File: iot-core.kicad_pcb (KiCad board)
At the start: 2 copper layers, 34.3 x 61 mm, 50 parts, among them P1 USB, P10 CONN_01X01, P11 CONN_01X01, P2 CONN_01X02, P3 CONN_01X16, P4 CONN_01X04, P5 CONN_01X16, P6 CONN_01X03, P7 CONN_01X03, P8 CONN_01X01, P9 CONN_01X01, SW1 RST, U1 LP2985LV, U2 STM32F103C8Tx, U3 ESP-07v2, Y1 8MHz

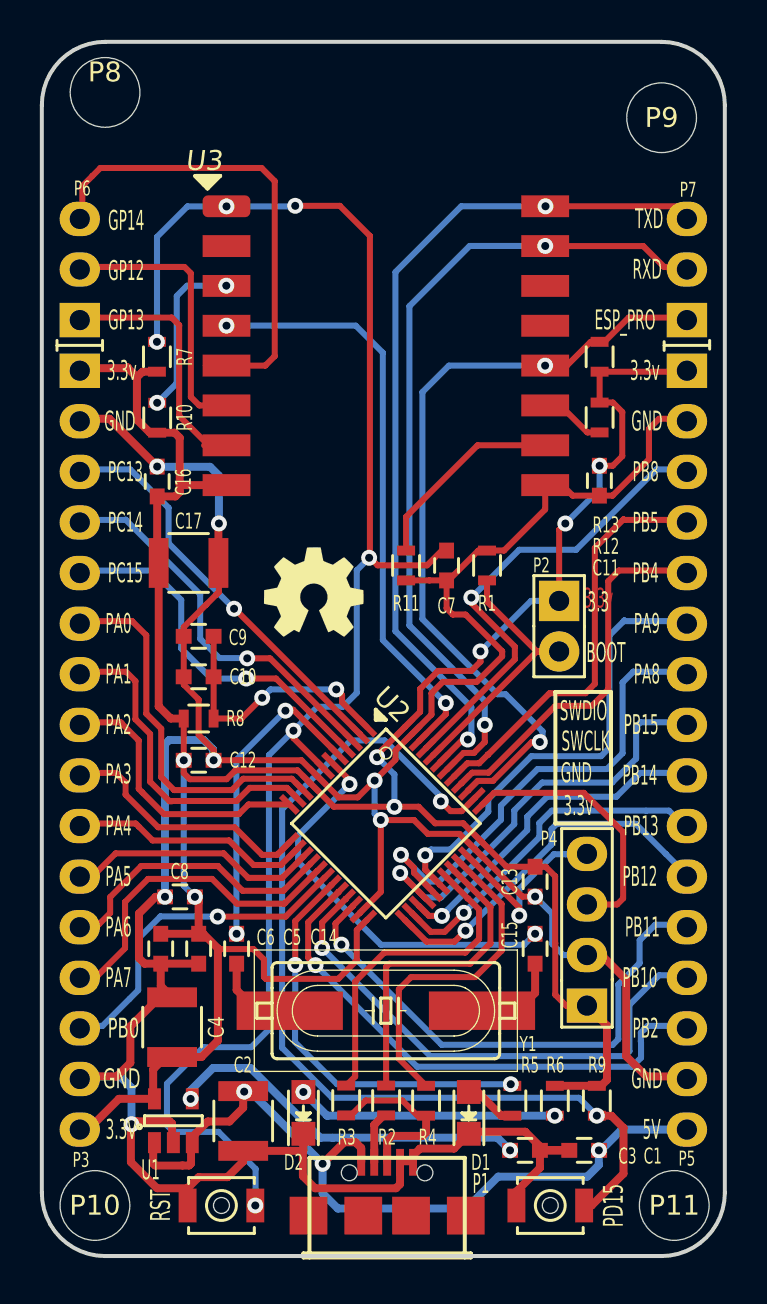
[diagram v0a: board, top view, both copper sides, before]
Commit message: Fix DAO DONG THACH ANH KHONG NOI GND, pin ESP_PRO to PB0, GPIO16 to PB11,DELETE header BOOT 0
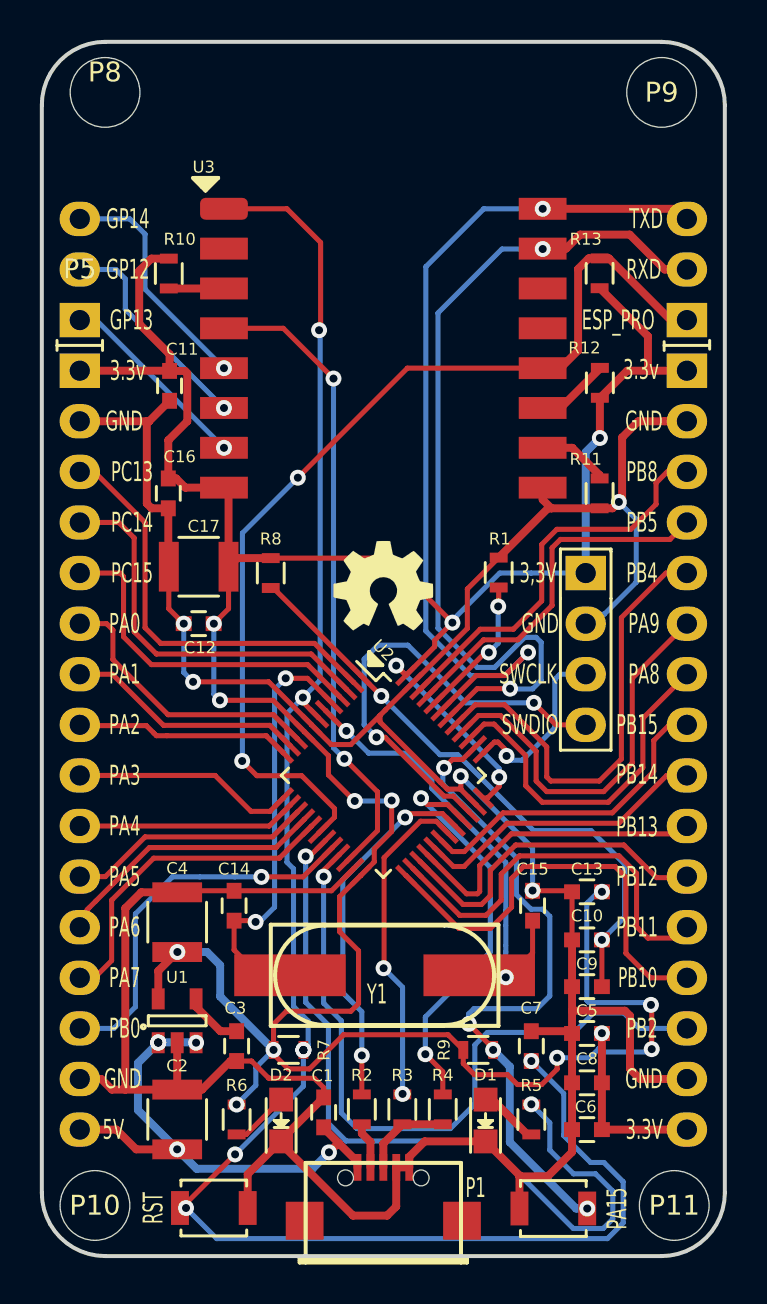
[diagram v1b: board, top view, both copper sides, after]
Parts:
- removed P2: CONN_01X02, Pin_Headers:Pin_Header_Straight_1x02
- removed PD15: SW_PUSH_SMALL_H, Buttons_Switches_SMD:SW_SPST_B3U-1000P-B
- removed SW1: RST, Buttons_Switches_SMD:SW_SPST_B3U-1000P-B
- added PA15: SW_PUSH_SMALL_H, Buttons_Switches_SMD:SW_SPST_B3U-1000P-B, F.Cu at (130.5, 133.5)
- added RST: RST, Buttons_Switches_SMD:SW_SPST_B3U-1000P-B, F.Cu at (113.4, 133.5)
- U2: footprint stm32f108:LQFP48 -> Housings_QFP:LQFP-48_7x7mm_Pitch0.5mm
- Y1: footprint crystal:crystal-HC49UP -> Crystal:HC49_sm
- moved R7 35.4 mm to (117.2, 125.5), turned to 180 degrees
- moved P3 30.5 mm to (137.2, 91.4)
- moved P5 30.5 mm to (106.7, 91.4)
- moved C9 26.3 mm to (132.1, 122.4)
- moved C7 24.5 mm to (129.3, 125.3), turned to 90 degrees
- moved C10 23.5 mm to (132.1, 120.0)
- moved C6 23.2 mm to (132.1, 129.5), turned to 0 degrees
- moved C8 22.5 mm to (132.1, 127.2)
- moved C11 22.1 mm to (111.2, 92.2)
- moved P4 21.7 mm to (132.1, 101.6), turned to 0 degrees
- moved C5 20.0 mm to (132.1, 124.7), turned to 0 degrees
- moved R6 16.0 mm to (114.6, 129.0)
- moved C3 15.4 mm to (114.6, 125.3), turned to 270 degrees
- moved C1 13.2 mm to (118.9, 128.7), turned to 90 degrees
- moved R11 10.4 mm to (132.8, 97.6)
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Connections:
- net IO-13 renamed PB2
- C14 pad 2: Net-(C14-Pad2) -> GNDREF
- C15 pad 2: Net-(C15-Pad2) -> GNDREF
- P3 pad 10: IO-7 -> PB15
- P3 pad 11: IO-8 -> PB14
- P3 pad 12: IO-9 -> PB13
- P3 pad 13: IO-10 -> PB12
- P3 pad 14: IO-11 -> PB10
- P3 pad 3: IO-0 -> PB9
- P3 pad 4: IO-1 -> PB8
- P3 pad 5: IO-2 -> PB5
- P3 pad 6: IO-3 -> PB4
- P3 pad 7: IO-4 -> PB3
- P3 pad 8: IO-5 -> PA9
- P3 pad 9: IO-6 -> PA8
- P5 pad 10: IO-17 -> PA4
- P5 pad 11: IO-16 -> PA5
- P5 pad 12: IO-15 -> PA6
- P5 pad 13: IO-14 -> PA7
- P5 pad 3: IO-24 -> PA13
- P5 pad 4: IO-23 -> PA14
- P5 pad 5: IO-22 -> PA15
- P5 pad 6: IO-21 -> PA0
- P5 pad 7: IO-20 -> PA1
- P5 pad 8: IO-19 -> PA2
- P5 pad 9: IO-18 -> PA3
- U2 pad 10: IO-3 -> PA0
- U2 pad 11: IO-4 -> PA1
- U2 pad 12: IO-5 -> PA2
- U2 pad 13: IO-6 -> PA3
- U2 pad 14: IO-7 -> PA4
- U2 pad 15: IO-8 -> PA5
- U2 pad 16: IO-9 -> PA6
- U2 pad 17: IO-10 -> PA7
- U2 pad 18: IO-11 -> ESP_PRO
- U2 pad 2: IO-0 -> PA13
- U2 pad 21: IO-14 -> PB10
- U2 pad 22: IO-15 -> GPIO16
- U2 pad 25: IO-16 -> PB12
- U2 pad 26: IO-17 -> PB13
- U2 pad 27: IO-18 -> PB14
- U2 pad 28: IO-19 -> PB15
- U2 pad 29: IO-20 -> PA8
- U2 pad 3: IO-1 -> PA14
- U2 pad 30: IO-21 -> PA9
- U2 pad 39: ESP_PRO -> PB3
- U2 pad 4: IO-2 -> PA15
- U2 pad 40: IO-22 -> PB4
- U2 pad 41: IO-23 -> PB5
- U2 pad 45: IO-24 -> PB8
- U2 pad 46: GPIO -> PB9
- U3 pad 4: GPIO -> GPIO16
- Y1 pad 1: Net-(C14-Pad2) -> /OSC_IN
- Y1 pad 2: Net-(C15-Pad2) -> /OSC_OUT
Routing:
- net PB10: track 0.00 -> 35.8 mm, vias 0 -> 2
- net +3V3: track 140.7 -> 173.3 mm, vias 8 -> 17
- net GPIO16: track 0.00 -> 32.4 mm, vias 0 -> 2
- net GPIO: track 29.8 -> 0.00 mm, vias 2 -> 0
- net IO-15: track 26.8 -> 0.00 mm, vias 2 -> 0
- net IO-14: track 26.7 -> 0.00 mm, vias 2 -> 0
- net IO-20: track 24.4 -> 0.00 mm, vias 2 -> 0
- net IO-24: track 23.9 -> 0.00 mm, vias 2 -> 0
- net IO-21: track 23.7 -> 0.00 mm, vias 2 -> 0
- net PB5: track 0.00 -> 23.0 mm
- net PB12: track 0.00 -> 21.9 mm
- net IO-19: track 21.9 -> 0.00 mm, vias 2 -> 0
- net PA13: track 0.00 -> 21.2 mm
- net IO-23: track 21.2 -> 0.00 mm
- net IO-0: track 20.5 -> 0.00 mm, vias 2 -> 0
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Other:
- net class Default: trace_width 0.3 -> 0.4
- rule trace_min: 0.3 -> 0.25
- board text added: "3,3V"
- board text removed: "3.3"
- board text removed: "BOOT"
